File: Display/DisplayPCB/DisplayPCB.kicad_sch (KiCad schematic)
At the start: 16 parts, among them IC1 MIC3490-3.0YM5-TR, IC2 TXU0104PWR, IC3 TXU0104PWR, J1 Conn_01x08, J3 Conn_01x06_Female

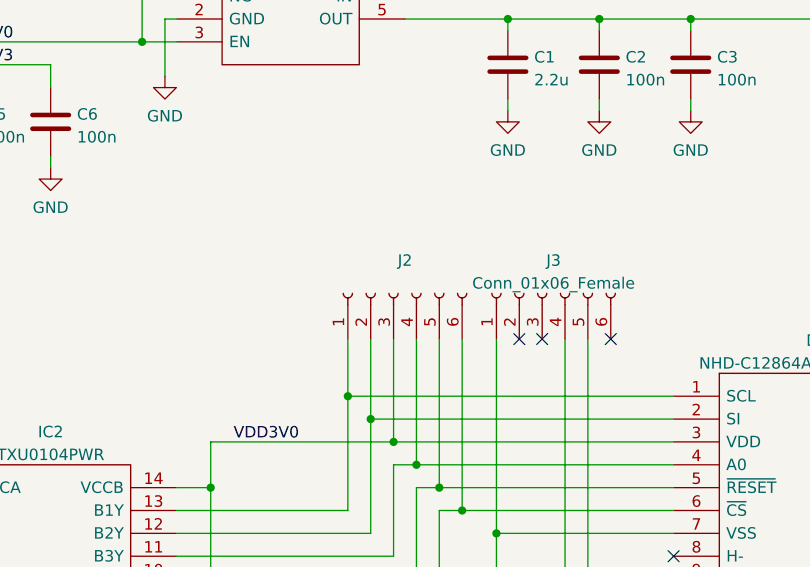
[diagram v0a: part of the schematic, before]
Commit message: Changed paths for linux
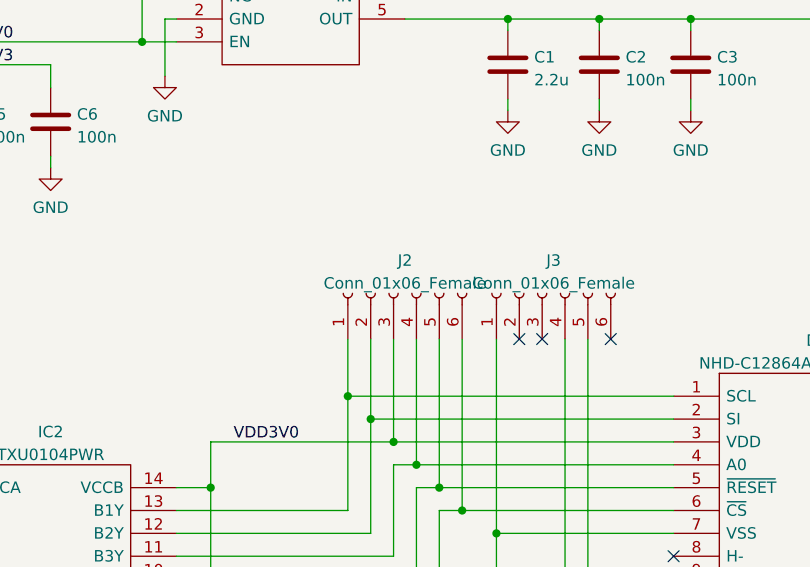
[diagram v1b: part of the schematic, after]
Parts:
- J2: value (none) -> Conn_01x06_Female; footprint (none) -> Connector_PinHeader_2.54mm:PinHeader_1x06_P2.54mm_Vertical
- J3: footprint (none) -> Connector_PinHeader_2.54mm:PinHeader_1x06_P2.54mm_Vertical
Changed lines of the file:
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@@
     (property "Reference" "J3" (id 0) (at 113.03 70.011 90))
     (property "Value" "Conn_01x06_Female" (id 1) (at 113.03 72.5479 90))
-    (property "Footprint" "" (id 2) (at 111.76 73.66 0)
+    (property "Footprint" "Connector_PinHeader_2.54mm:PinHeader_1x06_P2.54mm_Vertical" (id 2) (at 111.76 73.66 0)
       (effects (font (size 1.27 1.27)) hide)
     )
@@
     (in_bom yes) (on_board yes) (fields_autoplaced)
     (property "Reference" "J2" (id 0) (at 96.52 70.011 90))
-    (property "Value" "" (id 1) (at 96.52 72.5479 90))
-    (property "Footprint" "" (id 2) (at 95.25 73.66 0)
+    (property "Value" "Conn_01x06_Female" (id 1) (at 96.52 72.5479 90))
+    (property "Footprint" "Connector_PinHeader_2.54mm:PinHeader_1x06_P2.54mm_Vertical" (id 2) (at 95.25 73.66 0)
       (effects (font (size 1.27 1.27)) hide)
     )
